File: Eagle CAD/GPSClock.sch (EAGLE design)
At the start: 40 parts, among them IC3 LM1117, J1 AMP FCI 10103594-0001LF, J2 ISP, J3 POWER_JACKSUPER_BOMB_DIGITY, J4 BM06B-SRSS-TB, Q1 1A/60V/500mΩ, U1 CH340C, U3 AP2112-3.3V, U4 ATMEGA328P_TQFP, Y1 16MHz

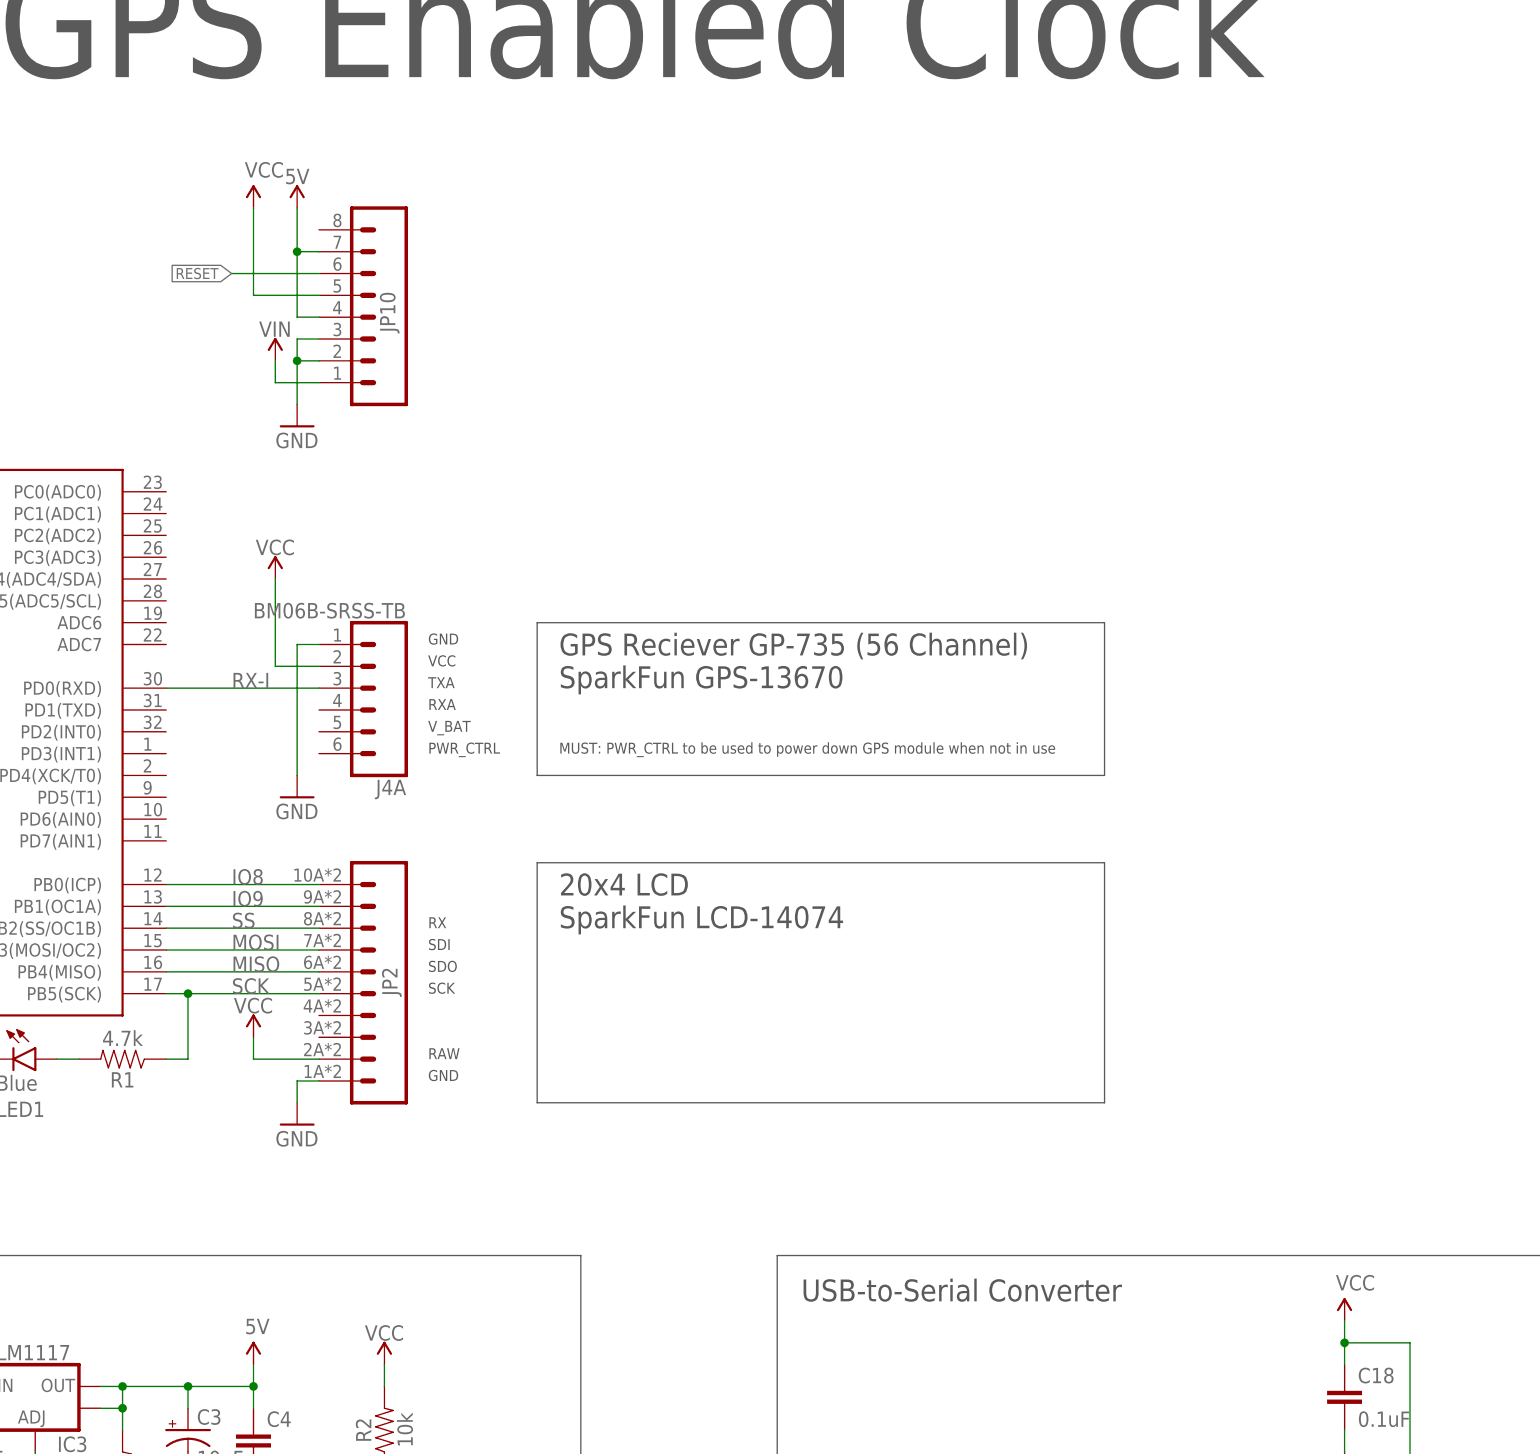
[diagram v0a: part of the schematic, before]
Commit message: Updated schematic with correct port for GPS Rx
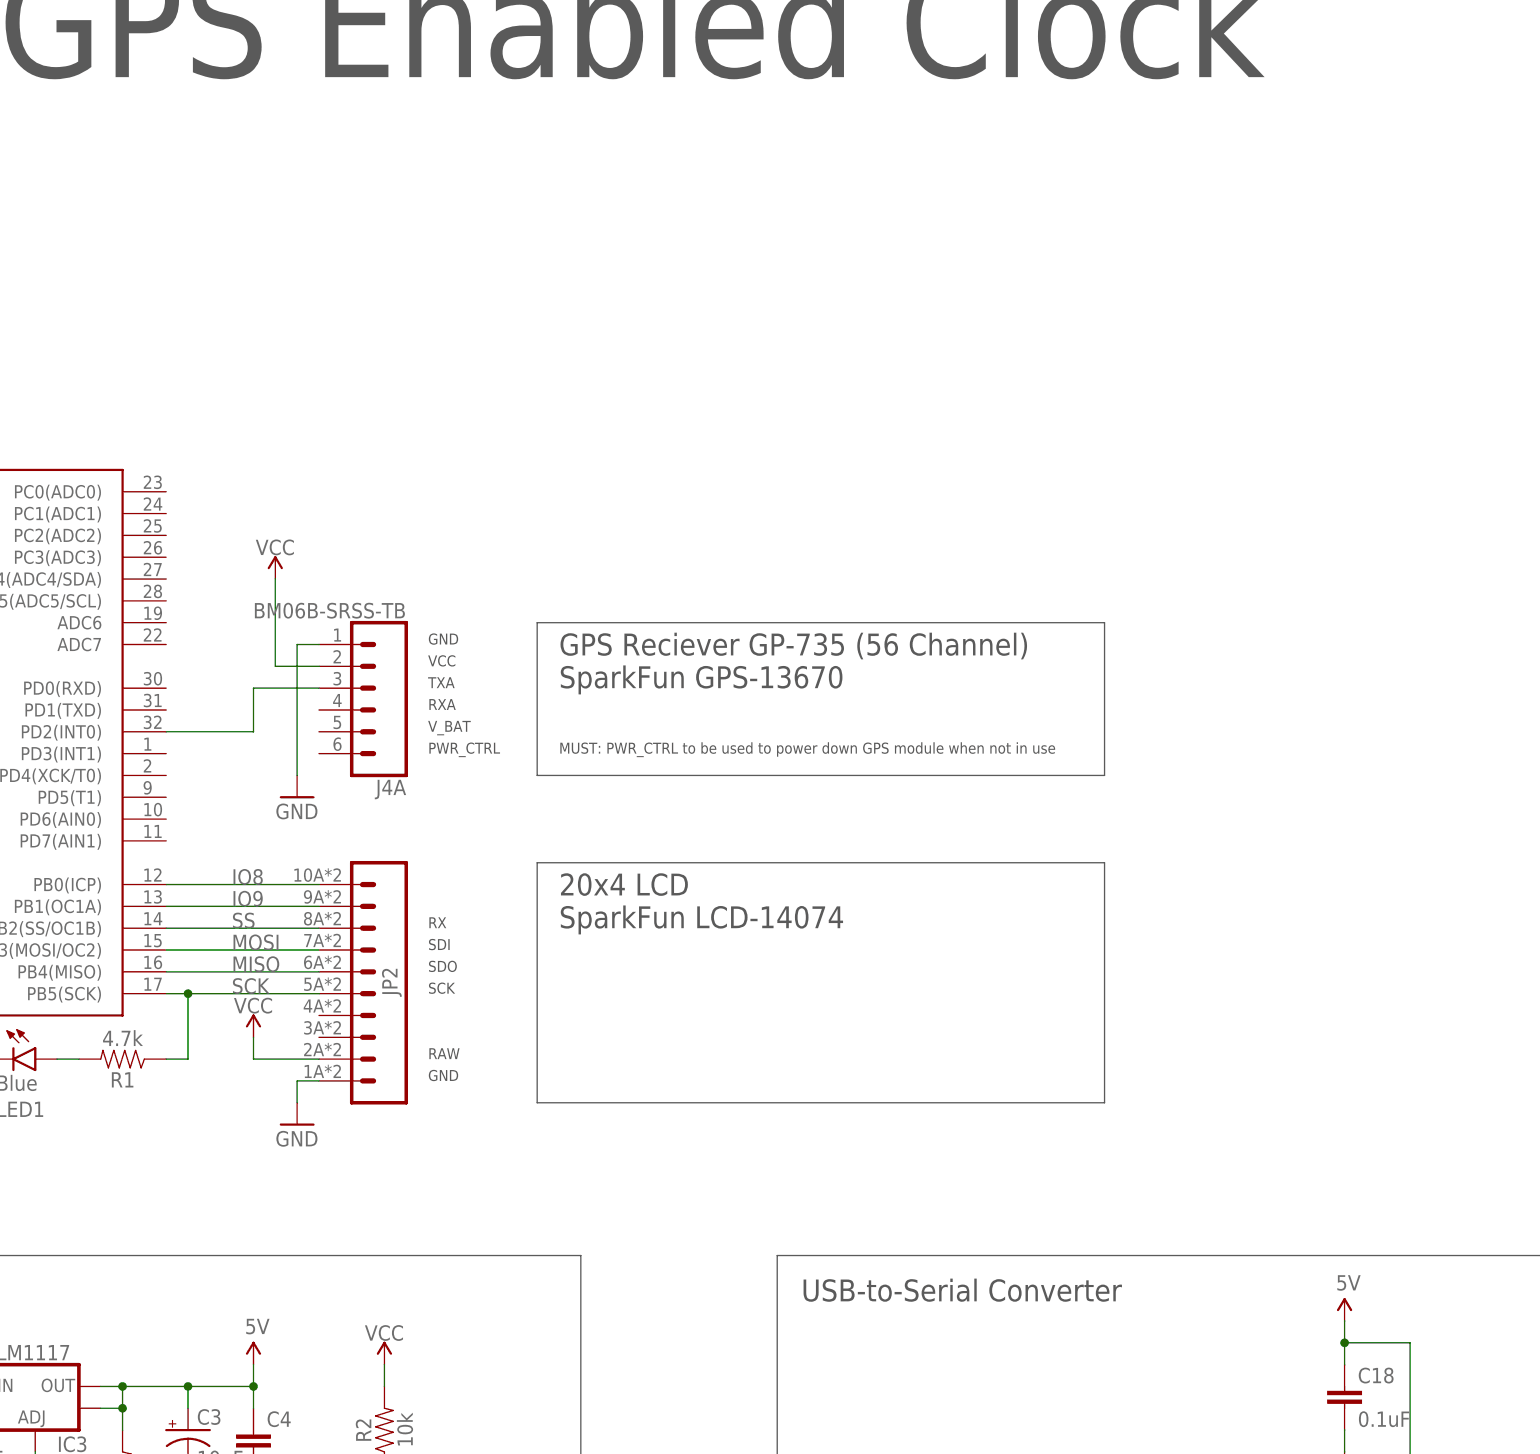
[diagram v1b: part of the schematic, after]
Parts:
- removed JP10: (no value), SparkFun-Connectors:CONN_08SMD-COMBO-FEMALE
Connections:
- new net N$7: J4A.3, U4.PD2(INT0)
- net 5V: now also C18.1, U1.VCC; no longer JP10.4, JP10.7
- net GND: no longer JP10.2, JP10.3
- net RESET: no longer JP10.6
- net RX-I: no longer J4A.3, U4.PD0(RXD)
- net VCC: no longer C18.1, JP10.5, U1.VCC
- net VIN: no longer JP10.1
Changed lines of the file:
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@@
 <attribute name="PROD_ID" value="CONN-11219"/>
-</part>
-<part name="JP10" library="SparkFun-Connectors" deviceset="CONN_08" device="SMD-COMBO-FEMALE">
-<attribute name="PROD_ID" value="CONN-10204"/>
 </part>
 <part name="Y1" library="SparkFun-Clocks" deviceset="RESONATOR-16MHZ" device="SMD_3.2X1.3" value="16MHz"/>
@@
 <part name="GND10" library="SparkFun-Aesthetics" deviceset="GND" device=""/>
 <part name="GND20" library="SparkFun-Aesthetics" deviceset="GND" device=""/>
-<part name="GND23" library="SparkFun-Aesthetics" deviceset="GND" device=""/>
-<part name="SUPPLY3" library="SparkFun-PowerSymbols" deviceset="5V" device=""/>
-<part name="SUPPLY5" library="SparkFun-PowerSymbols" deviceset="VIN" device=""/>
 <part name="LED2" library="SparkFun-LED" deviceset="LED-GREEN" device="_HIDDENSILK" value="GREEN">
 <attribute name="PROD_ID" value="DIO-09910"/>
@@
 <part name="R12" library="SparkFun-Resistors" deviceset="4.7KOHM" device="-0603-1/10W-1%" value="4.7k"/>
 <part name="C18" library="SparkFun-Capacitors" deviceset="0.1UF" device="-0603-25V-(+80/-20%)" value="0.1uF"/>
-<part name="SUPPLY1" library="SparkFun-Aesthetics" deviceset="VCC" device=""/>
 <part name="SUPPLY4" library="SparkFun-Aesthetics" deviceset="VCC" device=""/>
 <part name="SUPPLY9" library="SparkFun-Aesthetics" deviceset="VCC" device=""/>
@@
 <part name="J4" library="SparkFun-Connectors" deviceset="JST_6_PIN_HORIZONTAL" device="" value="BM06B-SRSS-TB"/>
 <part name="SUPPLY2" library="SparkFun-Aesthetics" deviceset="VCC" device=""/>
-<part name="SUPPLY6" library="SparkFun-Aesthetics" deviceset="VCC" device=""/>
 <part name="GND2" library="SparkFun" deviceset="GND" device=""/>
 <part name="SUPPLY8" library="SparkFun-PowerSymbols" deviceset="VCC" device=""/>
 <part name="GND15" library="SparkFun" deviceset="GND" device=""/>
 <part name="SUPPLY10" library="SparkFun-PowerSymbols" deviceset="VCC" device=""/>
+<part name="U$10" library="SparkFun-PowerSymbols" deviceset="5V" device=""/>
 </parts>
 <sheets>
@@
 <attribute name="PROD_ID" x="226.06" y="160.02" size="1.778" layer="96" rot="MR0" display="off"/>
 </instance>
-<instance part="JP10" gate="G$1" x="220.98" y="231.14" smashed="yes" rot="MR0">
-<attribute name="PROD_ID" x="220.98" y="231.14" size="1.778" layer="96" rot="MR0" display="off"/>
-<attribute name="VALUE" x="226.06" y="218.44" size="1.778" layer="96" rot="MR0"/>
-<attribute name="NAME" x="224.79" y="229.362" size="1.778" layer="95" font="vector" rot="R90"/>
-</instance>
 <instance part="Y1" gate="G$1" x="147.32" y="182.88" smashed="yes" rot="R270">
 <attribute name="NAME" x="146.05" y="177.546" size="1.778" layer="95" font="vector"/>
@@
 <instance part="GND20" gate="1" x="314.96" y="63.5" smashed="yes">
 <attribute name="VALUE" x="312.42" y="60.96" size="1.778" layer="96"/>
-</instance>
-<instance part="GND23" gate="1" x="213.36" y="218.44" smashed="yes">
-<attribute name="VALUE" x="210.82" y="215.9" size="1.778" layer="96"/>
-</instance>
-<instance part="SUPPLY3" gate="G$1" x="213.36" y="243.84" smashed="yes">
-<attribute name="VALUE" x="213.36" y="246.634" size="1.778" layer="96" align="bottom-center"/>
-</instance>
-<instance part="SUPPLY5" gate="G$1" x="210.82" y="226.06" smashed="yes" rot="MR0">
-<attribute name="VALUE" x="210.82" y="228.854" size="1.778" layer="96" rot="MR0" align="bottom-center"/>
 </instance>
 <instance part="LED2" gate="G$1" x="223.52" y="91.44" smashed="yes">
@@
 <attribute name="NAME" x="336.804" y="107.061" size="1.778" layer="95"/>
 <attribute name="VALUE" x="336.804" y="101.981" size="1.778" layer="96"/>
-</instance>
-<instance part="SUPPLY1" gate="G$1" x="335.28" y="114.3" smashed="yes">
-<attribute name="VALUE" x="334.264" y="117.856" size="1.778" layer="96"/>
 </instance>
 <instance part="SUPPLY4" gate="G$1" x="370.84" y="114.3" smashed="yes">
@@
 <attribute name="VALUE" x="225.044" y="54.356" size="1.778" layer="96"/>
 </instance>
-<instance part="SUPPLY6" gate="G$1" x="208.28" y="243.84" smashed="yes">
-<attribute name="VALUE" x="207.264" y="247.396" size="1.778" layer="96"/>
-</instance>
 <instance part="GND2" gate="1" x="213.36" y="137.16" smashed="yes">
 <attribute name="VALUE" x="210.82" y="134.62" size="1.778" layer="96"/>
@@
 <instance part="SUPPLY10" gate="G$1" x="210.82" y="200.66" smashed="yes">
 <attribute name="VALUE" x="210.82" y="203.454" size="1.778" layer="96" align="bottom-center"/>
+</instance>
+<instance part="U$10" gate="G$1" x="335.28" y="114.3" smashed="yes">
+<attribute name="VALUE" x="334.264" y="117.856" size="1.778" layer="96" font="vector"/>
 </instance>
 </instances>
@@
 <nets>
 <net name="RX-I" class="0">
-<segment>
-<wire x1="215.9" y1="187.96" x2="198.12" y2="187.96" width="0.1524" layer="91"/>
-<label x="205.74" y="187.96" size="1.778" layer="95" font="vector"/>
-<pinref part="U4" gate="U$1" pin="PD0(RXD)"/>
-<pinref part="J4" gate="A" pin="3"/>
-</segment>
 <segment>
 <pinref part="U1" gate="U1" pin="TXO"/>
@@
 </segment>
 <segment>
-<pinref part="JP10" gate="G$1" pin="7"/>
-<wire x1="215.9" y1="238.76" x2="213.36" y2="238.76" width="0.1524" layer="91"/>
-<pinref part="SUPPLY3" gate="G$1" pin="5V"/>
-<wire x1="213.36" y1="238.76" x2="213.36" y2="243.84" width="0.1524" layer="91"/>
-<junction x="213.36" y="238.76"/>
-<pinref part="JP10" gate="G$1" pin="4"/>
-<wire x1="213.36" y1="231.14" x2="215.9" y2="231.14" width="0.1524" layer="91"/>
-<wire x1="213.36" y1="231.14" x2="213.36" y2="238.76" width="0.1524" layer="91"/>
-</segment>
-<segment>
 <pinref part="U3" gate="G$1" pin="EN"/>
 <wire x1="193.04" y1="43.18" x2="190.5" y2="43.18" width="0.1524" layer="91"/>
@@
 <wire x1="190.5" y1="50.8" x2="190.5" y2="48.26" width="0.1524" layer="91"/>
 </segment>
+<segment>
+<pinref part="C18" gate="G$1" pin="1"/>
+<wire x1="335.28" y1="109.22" x2="335.28" y2="111.76" width="0.1524" layer="91"/>
+<wire x1="335.28" y1="114.3" x2="335.28" y2="111.76" width="0.1524" layer="91"/>
+<pinref part="U1" gate="U1" pin="VCC"/>
+<wire x1="347.98" y1="88.9" x2="342.9" y2="88.9" width="0.1524" layer="91"/>
+<wire x1="342.9" y1="88.9" x2="342.9" y2="111.76" width="0.1524" layer="91"/>
+<wire x1="342.9" y1="111.76" x2="335.28" y2="111.76" width="0.1524" layer="91"/>
+<junction x="335.28" y="111.76"/>
+<pinref part="U$10" gate="G$1" pin="5V"/>
+</segment>
 </net>
 <net name="GND" class="0">
@@
 <pinref part="GND1" gate="1" pin="GND"/>
 <pinref part="J2" gate="G$1" pin="6"/>
-</segment>
-<segment>
-<wire x1="215.9" y1="226.06" x2="213.36" y2="226.06" width="0.1524" layer="91"/>
-<pinref part="JP10" gate="G$1" pin="2"/>
-<pinref part="GND23" gate="1" pin="GND"/>
-<wire x1="213.36" y1="220.98" x2="213.36" y2="226.06" width="0.1524" layer="91"/>
-<junction x="213.36" y="226.06"/>
-<wire x1="215.9" y1="228.6" x2="213.36" y2="228.6" width="0.1524" layer="91"/>
-<pinref part="JP10" gate="G$1" pin="3"/>
-<wire x1="213.36" y1="228.6" x2="213.36" y2="226.06" width="0.1524" layer="91"/>
 </segment>
 <segment>
@@
 <pinref part="J2" gate="G$1" pin="5"/>
 <label x="99.06" y="147.32" size="1.27" layer="95" font="vector" rot="R180" xref="yes"/>
-</segment>
-<segment>
-<wire x1="215.9" y1="236.22" x2="205.74" y2="236.22" width="0.1524" layer="91"/>
-<pinref part="JP10" gate="G$1" pin="6"/>
-<label x="205.74" y="236.22" size="1.27" layer="95" font="vector" rot="R180" xref="yes"/>
 </segment>
 <segment>
@@
 <net name="VIN" class="0">
 <segment>
-<wire x1="210.82" y1="223.52" x2="215.9" y2="223.52" width="0.1524" layer="91"/>
-<pinref part="JP10" gate="G$1" pin="1"/>
-<pinref part="SUPPLY5" gate="G$1" pin="VIN"/>
-<wire x1="210.82" y1="223.52" x2="210.82" y2="226.06" width="0.1524" layer="91"/>
-</segment>
-<segment>
 <wire x1="175.26" y1="106.68" x2="172.72" y2="106.68" width="0.1524" layer="91"/>
 <wire x1="172.72" y1="104.14" x2="172.72" y2="106.68" width="0.1524" layer="91"/>
@@
 </net>
 <net name="VCC" class="0">
-<segment>
-<pinref part="C18" gate="G$1" pin="1"/>
-<wire x1="335.28" y1="109.22" x2="335.28" y2="111.76" width="0.1524" layer="91"/>
-<pinref part="SUPPLY1" gate="G$1" pin="VCC"/>
-<wire x1="335.28" y1="114.3" x2="335.28" y2="111.76" width="0.1524" layer="91"/>
-<pinref part="U1" gate="U1" pin="VCC"/>
-<wire x1="347.98" y1="88.9" x2="342.9" y2="88.9" width="0.1524" layer="91"/>
-<wire x1="342.9" y1="88.9" x2="342.9" y2="111.76" width="0.1524" layer="91"/>
-<wire x1="342.9" y1="111.76" x2="335.28" y2="111.76" width="0.1524" layer="91"/>
-<junction x="335.28" y="111.76"/>
-</segment>
 <segment>
 <wire x1="370.84" y1="114.3" x2="370.84" y2="111.76" width="0.1524" layer="91"/>
@@
 </segment>
 <segment>
-<wire x1="215.9" y1="233.68" x2="208.28" y2="233.68" width="0.1524" layer="91"/>
-<pinref part="JP10" gate="G$1" pin="5"/>
-<wire x1="208.28" y1="243.84" x2="208.28" y2="233.68" width="0.1524" layer="91"/>
-<pinref part="SUPPLY6" gate="G$1" pin="VCC"/>
-</segment>
-<segment>
 <pinref part="JP2" gate="G$1" pin="2"/>
 <pinref part="SUPPLY8" gate="G$1" pin="VCC"/>
@@
 </segment>
 </net>
+<net name="N$7" class="0">
+<segment>
+<pinref part="U4" gate="U$1" pin="PD2(INT0)"/>
+<wire x1="198.12" y1="182.88" x2="208.28" y2="182.88" width="0.1524" layer="91"/>
+<pinref part="J4" gate="A" pin="3"/>
+<wire x1="208.28" y1="182.88" x2="208.28" y2="187.96" width="0.1524" layer="91"/>
+<wire x1="208.28" y1="187.96" x2="215.9" y2="187.96" width="0.1524" layer="91"/>
+</segment>
+</net>
